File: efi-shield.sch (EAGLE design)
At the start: 117 parts, among them J1 PWMH, J10 MOLEX-85505-5002, J2 PWMI, J3 COMM, J4 PWR, J5 ADCL, J6 ADCH, J7 AMPSEAL-23POS-HEADER, J8 SPI, J9 MOLEX-85505-5002, Q1 PN2222A, Q2 FJPF13009, Q3 PN2222A, Q4 PN2222A, Q5 PN2222A, Q6 PN2222A, SW1 CTS-204-211ST, U1 TXS0104E, U10 MCP2551-I/SN, U2 TXS0104E, U3 MCP3304, U4 MCP6024, U5 MCP6024, U6 MCP6022, U7 NE555DR, U8 MCP4142-104, U9 MCP4142-103

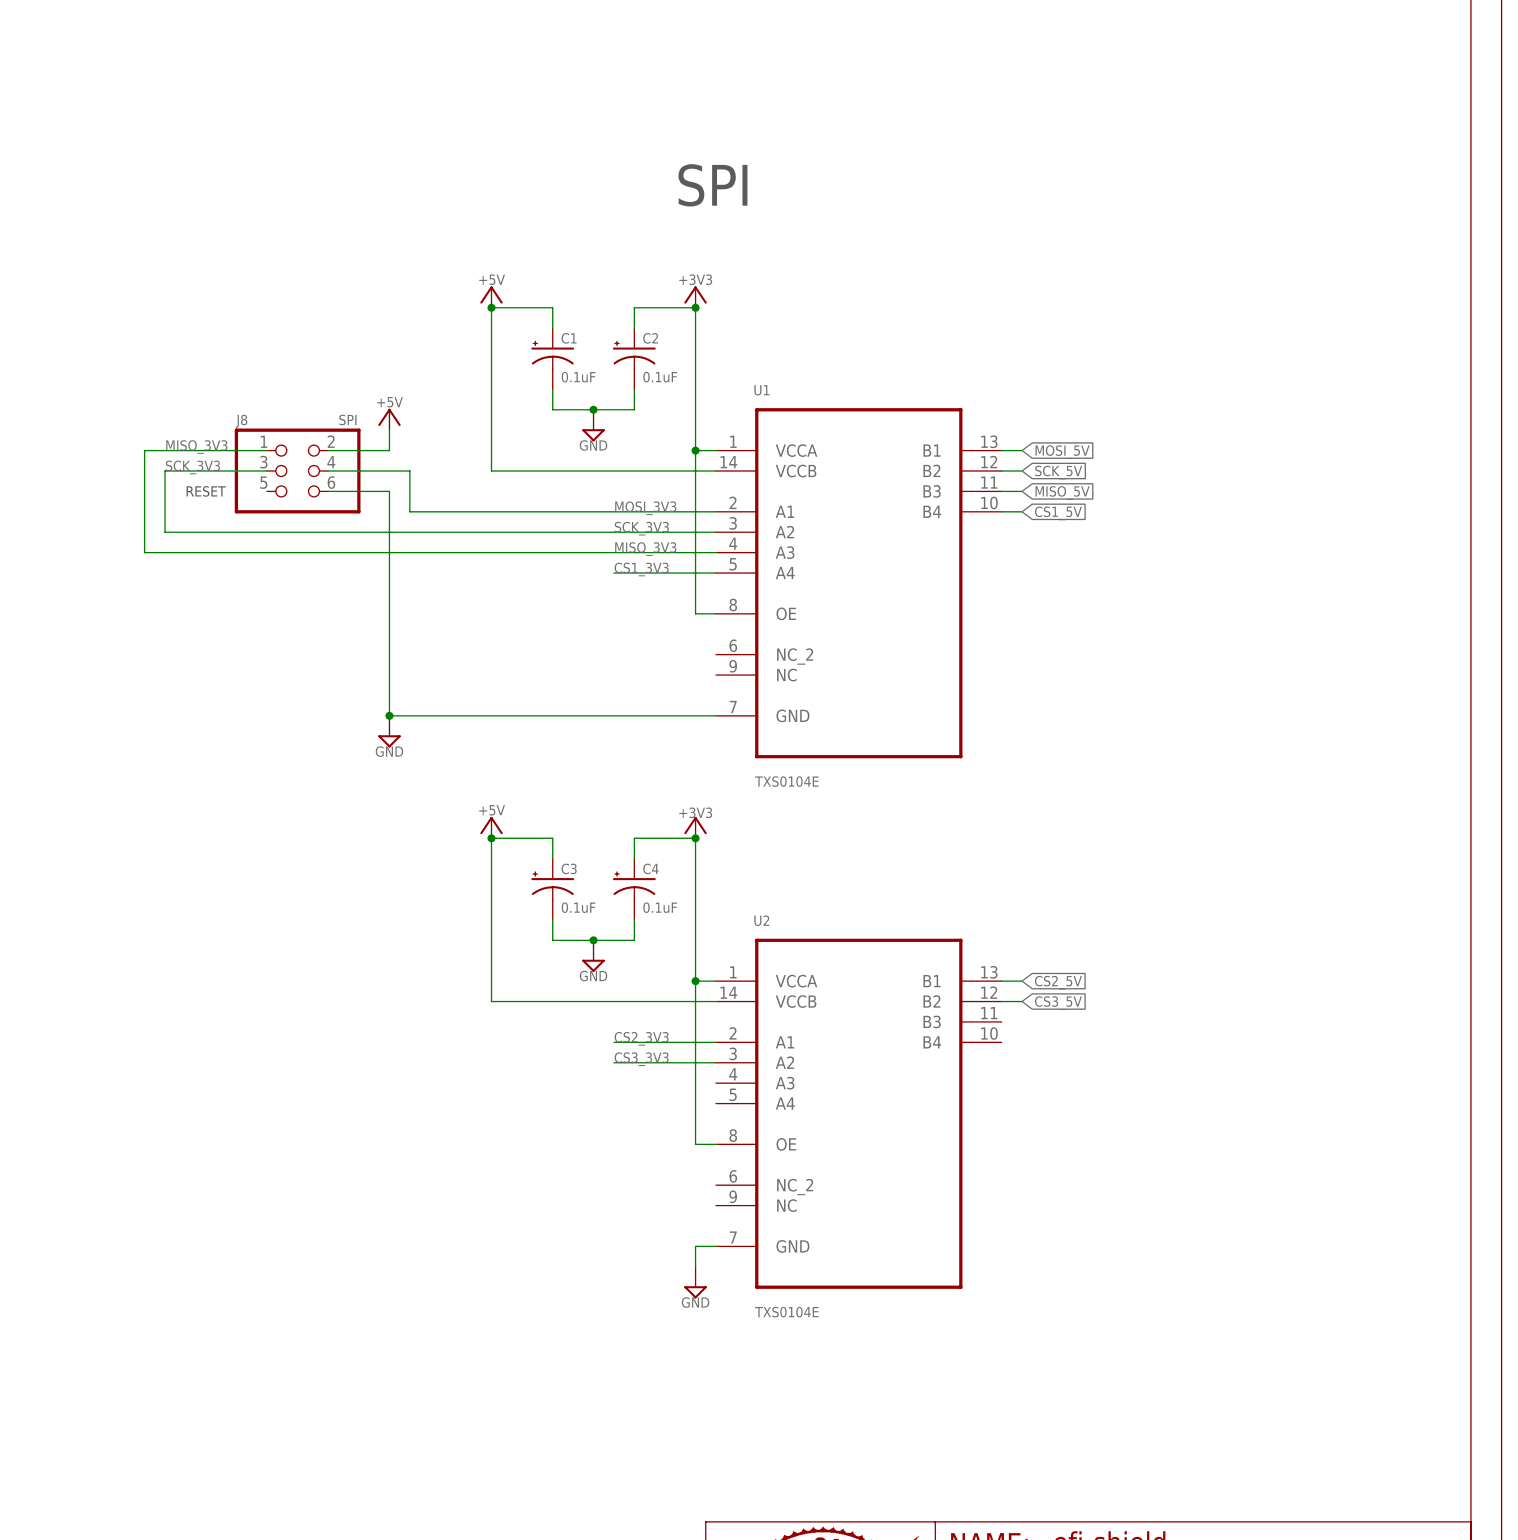
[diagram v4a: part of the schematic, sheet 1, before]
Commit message: Test points and 0ohm filter resistors.
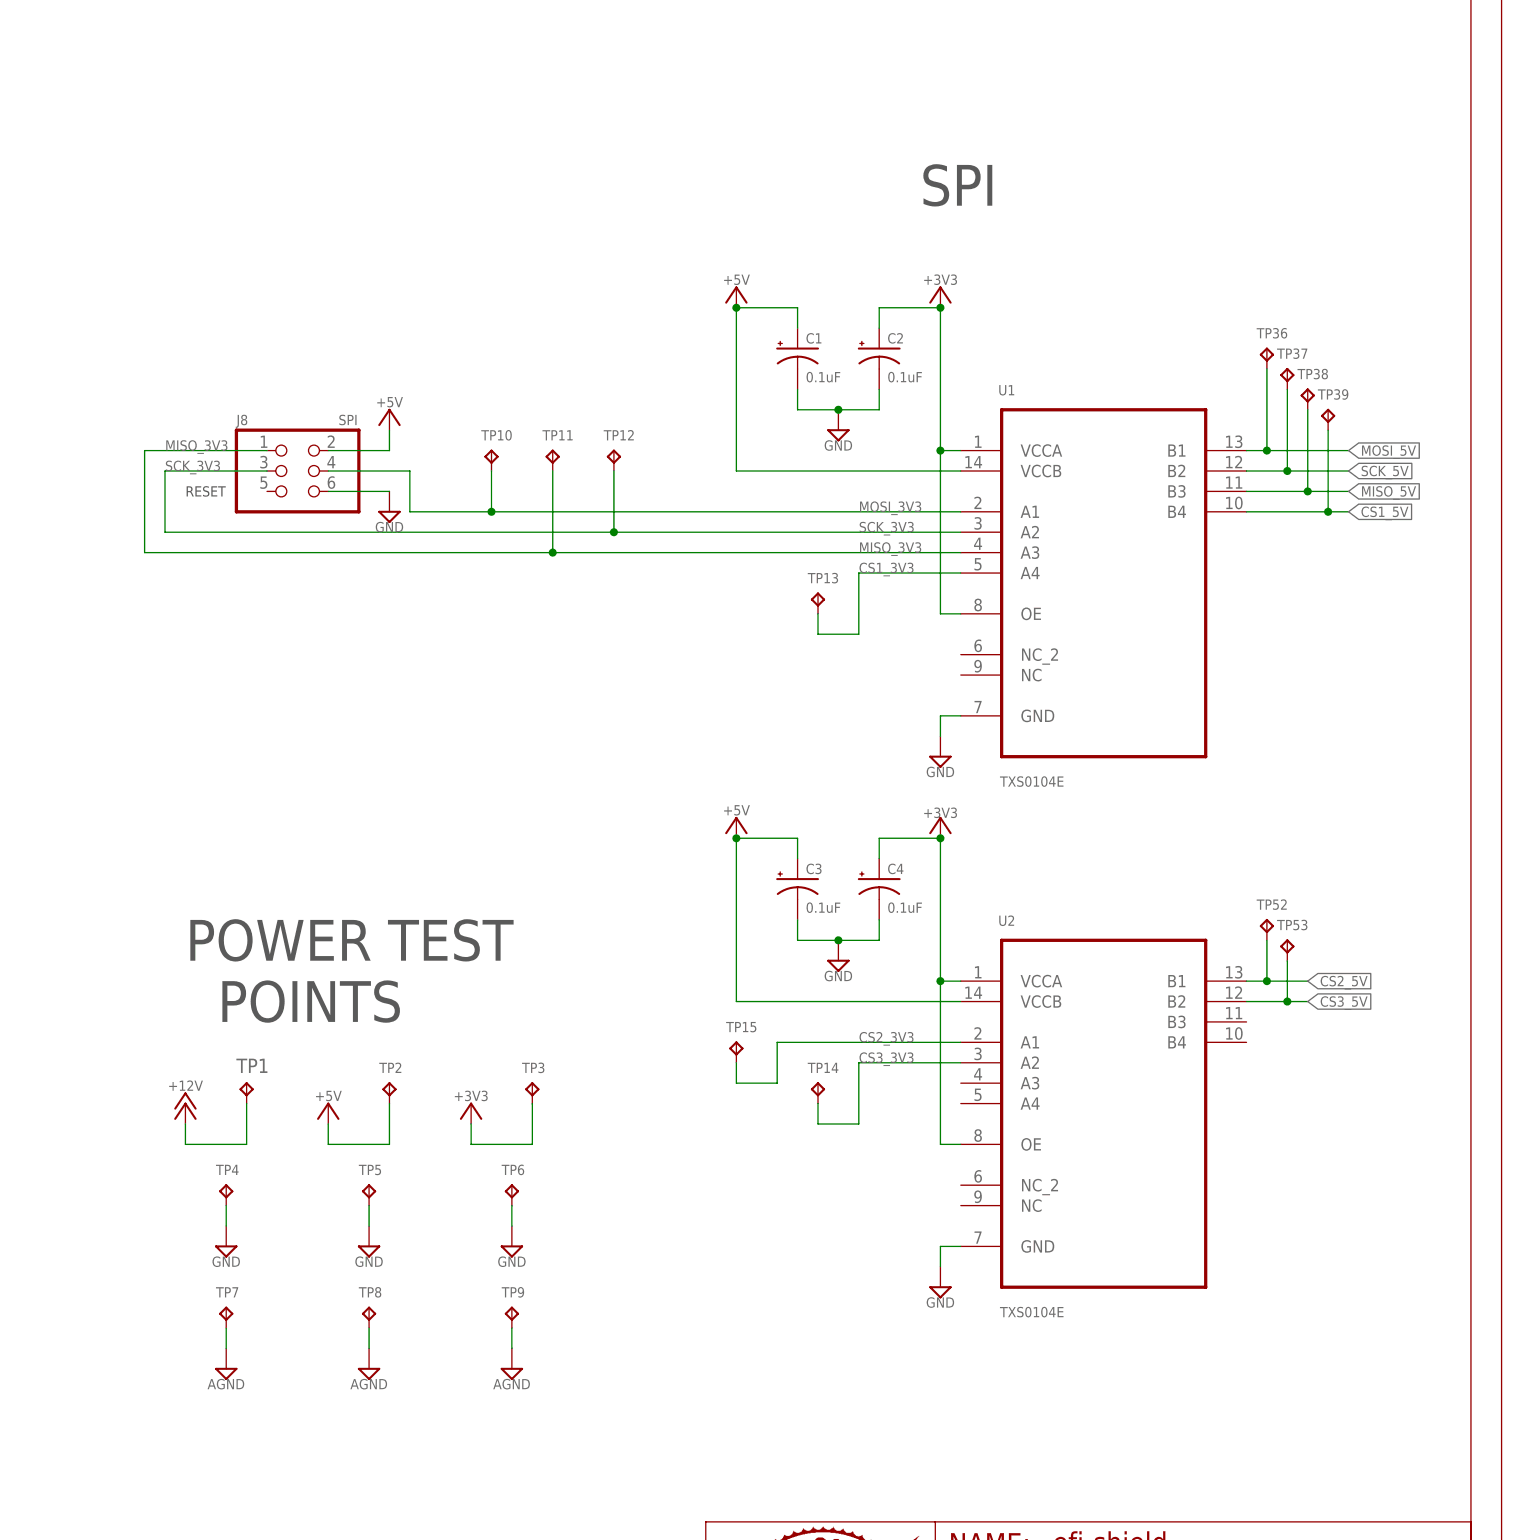
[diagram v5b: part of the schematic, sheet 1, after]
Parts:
- added R37, R38, R39, R40, R41, R42, R43, R44, R45: 0Ω, cpsmv:RES-JKE
- added TP1, TP10, TP11, TP12, TP13, TP14, TP15, TP16, TP17, TP18, TP19, TP2, TP20, TP21, TP22, TP23, TP24, TP25, TP26, TP27, TP28, TP29, TP3, TP30, TP31, TP32, TP33, TP34, TP35, TP36, TP37, TP38, TP39, TP4, TP40, TP41, TP42, TP43, TP44, TP45, TP46, TP47, TP48, TP49, TP5, TP50, TP51, TP52, TP53, TP6, TP7, TP8, TP9: (no value), cpsmv:TEST-POINT
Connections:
- new net ECT_ADC: R40.2, U3.CH3
- new net IAT_ADC: R39.2, U3.CH2
- new net MAP_ADC: R37.2, U3.CH0
- new net N$45: R45.2, U7.TRIG
- new net O2_ADC: R41.2, U3.CH4
- new net SPRA1ADC: R42.2, U3.CH5
- new net SPRA2ADC: R43.2, U3.CH6
- new net SPRA3ADC: R44.2, U3.CH7
- new net TPS_ADC: R38.2, U3.CH1
- net +12V: now also TP1.TP
- net +3V3: now also TP3.TP
- net +5V: now also TP2.TP
- net AGND: now also TP7.TP, TP8.TP, TP9.TP
- net CANH: now also TP44.TP
- net CANL: now also TP45.TP
- net CAN_RX: now also TP47.TP
- net CAN_TX: now also TP46.TP
- net CS1_3V3: now also TP13.TP
- net CS1_5V: now also TP39.TP
- net CS2_3V3: now also TP15.TP
- net CS2_5V: now also TP52.TP
- net CS3_3V3: now also TP14.TP
- net CS3_5V: now also TP53.TP
- net ECT: now also TP26.TP
- net ECT_FIL: now also R40.1, TP27.TP; no longer U3.CH3
- net FUEL: now also TP16.TP
- net FUEL_LED: now also TP49.TP
- net GND: now also TP4.TP, TP5.TP, TP6.TP
- net HALL: now also TP40.TP
- net HALL_FIL: now also R45.1, TP41.TP; no longer U7.TRIG
- net IAT: now also TP24.TP
- net IAT_FIL: now also R39.1, TP25.TP; no longer U3.CH2
- net KILL_SW_LED: now also TP51.TP
- net MAP: now also TP20.TP
- net MAP_FIL: now also R37.1, TP21.TP; no longer U3.CH0
- net MISO_3V3: now also TP11.TP
- net MISO_5V: now also TP38.TP
- net MOSI_3V3: now also TP10.TP
- net MOSI_5V: now also TP36.TP
- net N$38: now also TP19.TP
- net N$39: now also TP17.TP
- net O2: now also TP28.TP
- net O2_FIL: now also R41.1, TP29.TP; no longer U3.CH4
- net REV_LIMIT_LED: now also TP50.TP
- net SCK_3V3: now also TP12.TP
- net SCK_5V: now also TP37.TP
- net SPARK: now also TP18.TP
- net SPARK_LED: now also TP48.TP
- net SPR_A1: now also TP30.TP
- net SPR_A1_FIL: now also R42.1, TP31.TP; no longer U3.CH5
- net SPR_A2: now also TP32.TP
- net SPR_A2_FIL: now also R43.1, TP33.TP; no longer U3.CH6
- net SPR_A3: now also TP34.TP
- net SPR_A3_FIL: now also R44.1, TP35.TP; no longer U3.CH7
- net TACH_3V3: now also TP43.TP
- net TACH_5V: now also TP42.TP
- net TPS: now also TP22.TP
- net TPS_FIL: now also R38.1, TP23.TP; no longer U3.CH1
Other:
- note added: "LAYOUT NOTE: Place CAN termination as close as possible to RJ45 connectors for best CAN performance."
- note added: "POWER TEST POINTS"
- moved on the sheet: C1, C2, C24, C3, C4, Q1, Q2, Q7, R1, R31, R32, U1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

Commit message: Minor updates + schematic PDF.
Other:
- note added: "RJ45 CONNECTORS"
- note added: "TERMINATION"
- note added: "TRANSCEIVER"
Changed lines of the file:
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@@
 CANRX
 CANTX</text>
-<text x="139.7" y="193.04" size="5.08" layer="97">ARDUINO DUE</text>
-<text x="43.18" y="193.04" size="5.08" layer="97">AMPSEAL </text>
+<text x="139.7" y="193.04" size="5.08" layer="97" font="vector">ARDUINO DUE</text>
+<text x="43.18" y="193.04" size="5.08" layer="97" font="vector">AMPSEAL </text>
 <text x="223.52" y="157.48" size="1.27" layer="97" align="center-left">RESET</text>
-<text x="314.96" y="193.04" size="5.08" layer="97">SPI</text>
-<text x="20.32" y="99.06" size="5.08" layer="97">SPARE INPUTS</text>
+<text x="314.96" y="193.04" size="5.08" layer="97" font="vector">SPI</text>
+<text x="20.32" y="99.06" size="5.08" layer="97" font="vector">SPARE INPUTS</text>
 <text x="336.55" y="15.24" size="2.54" layer="94" font="vector">Alex Pink</text>
 <text x="361.95" y="5.08" size="2.54" layer="94" font="vector">01</text>
 <text x="334.01" y="20.32" size="2.54" layer="94" font="vector">Connectors &amp; SPI</text>
-<text x="223.52" y="91.44" size="5.08" layer="97">POWER TEST
+<text x="223.52" y="91.44" size="5.08" layer="97" font="vector">POWER TEST
   POINTS</text>
 </plain>
@@
 <description>ACTUATORS</description>
 <plain>
-<text x="190.5" y="186.69" size="5.08" layer="97">FUEL</text>
+<text x="190.5" y="186.69" size="5.08" layer="97" font="vector">FUEL</text>
 <text x="336.55" y="15.24" size="2.54" layer="94" font="vector">Alex Pink</text>
 <text x="361.95" y="5.08" size="2.54" layer="94" font="vector">01</text>
 <text x="334.01" y="20.32" size="2.54" layer="94" font="vector">Actutators</text>
-<text x="187.96" y="123.19" size="5.08" layer="97">SPARK</text>
+<text x="187.96" y="123.19" size="5.08" layer="97" font="vector">SPARK</text>
 </plain>
 <instances>
@@
 <wire x1="194.31" y1="135.89" x2="194.31" y2="127" width="0.1524" layer="97"/>
 <wire x1="194.31" y1="127" x2="193.04" y2="125.73" width="0.1524" layer="97"/>
-<text x="124.46" y="203.2" size="5.08" layer="97">LOW PASS FILTERS</text>
-<text x="297.18" y="175.26" size="5.08" layer="97">ADC</text>
+<text x="124.46" y="203.2" size="5.08" layer="97" font="vector">LOW PASS FILTERS</text>
+<text x="297.18" y="175.26" size="5.08" layer="97" font="vector">ADC</text>
 <text x="336.55" y="15.24" size="2.54" layer="94" font="vector">Alex Pink</text>
 <text x="361.95" y="5.08" size="2.54" layer="94" font="vector">01</text>
@@
 <text x="361.95" y="5.08" size="2.54" layer="94" font="vector">01</text>
 <text x="334.01" y="20.32" size="2.54" layer="94" font="vector">Tach</text>
-<text x="60.96" y="198.12" size="5.08" layer="97">LOW PASS FILTER</text>
+<text x="60.96" y="198.12" size="5.08" layer="97" font="vector">LOW PASS FILTER</text>
 <text x="55.88" y="185.42" size="1.27" layer="97" font="vector" align="top-left">LAYOUT NOTE:
 Place decoupling caps
@@
 <wire x1="158.75" y1="189.23" x2="158.75" y2="177.8" width="0.1524" layer="97"/>
 <wire x1="158.75" y1="177.8" x2="157.48" y2="176.53" width="0.1524" layer="97"/>
-<text x="271.78" y="134.62" size="5.08" layer="97">555 TIMER</text>
-<text x="165.1" y="198.12" size="5.08" layer="97">   DIGITAL
+<text x="271.78" y="134.62" size="5.08" layer="97" font="vector">555 TIMER</text>
+<text x="165.1" y="198.12" size="5.08" layer="97" font="vector">   DIGITAL
 POTENTIOMETERS</text>
 <text x="274.32" y="76.2" size="1.27" layer="97" font="vector" align="top-left">This capacitor should be
@@
 <wire x1="171.45" y1="118.11" x2="171.45" y2="106.68" width="0.1524" layer="97"/>
 <wire x1="171.45" y1="106.68" x2="170.18" y2="105.41" width="0.1524" layer="97"/>
+<text x="124.46" y="170.18" size="5.08" layer="97" font="vector">TRANSCEIVER</text>
+<text x="167.64" y="81.28" size="5.08" layer="97" font="vector">TERMINATION</text>
+<text x="233.68" y="190.5" size="5.08" layer="97" font="vector">RJ45 CONNECTORS</text>
 </plain>
 <instances>
@@
 <text x="361.95" y="5.08" size="2.54" layer="94" font="vector">01</text>
 <text x="334.01" y="20.32" size="2.54" layer="94" font="vector">LEDs</text>
-<text x="93.98" y="147.32" size="5.08" layer="97">POWER</text>
-<text x="180.34" y="170.18" size="5.08" layer="97">SPARK LED</text>
-<text x="180.34" y="129.54" size="5.08" layer="97">FUEL LED</text>
-<text x="284.48" y="170.18" size="5.08" layer="97">REV LIMIT LED</text>
-<text x="284.48" y="129.54" size="5.08" layer="97">KILLSWITCH LED</text>
+<text x="93.98" y="147.32" size="5.08" layer="97" font="vector">POWER</text>
+<text x="180.34" y="170.18" size="5.08" layer="97" font="vector">SPARK LED</text>
+<text x="180.34" y="129.54" size="5.08" layer="97" font="vector">FUEL LED</text>
+<text x="284.48" y="170.18" size="5.08" layer="97" font="vector">REV LIMIT LED</text>
+<text x="284.48" y="129.54" size="5.08" layer="97" font="vector">KILLSWITCH LED</text>
 </plain>
 <instances>

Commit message: Initial PCB commit.
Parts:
- removed U$1, U$2, U$3, U$4, U$5, U$6: CPSMV-FRAME, cpsmv:CPSMV-FRAME
- Q7: value (none) -> ISL9V5036P3_F085
- TP1: value (none) -> +12V
- TP10: value (none) -> MOSI_3V3
- TP11: value (none) -> MISO_3V3
- TP12: value (none) -> SCK_3V3
- TP13: value (none) -> CS1_3V3
- TP14: value (none) -> CS3_3V3
- TP15: value (none) -> CS2_3V3
- TP16: value (none) -> FUEL
- TP17: value (none) -> FUEL_E
- TP18: value (none) -> SPARK
- TP19: value (none) -> SPARK_E
- TP2: value (none) -> +5V
- TP20: value (none) -> MAP
- TP21: value (none) -> MAP_FIL
- TP22: value (none) -> TPS
- TP23: value (none) -> TPS_FIL
- TP24: value (none) -> IAT
- TP25: value (none) -> IAT_FIL
- TP26: value (none) -> ECT
- TP27: value (none) -> ECT_FIL
- TP28: value (none) -> O2
- TP29: value (none) -> O2_FIL
- TP3: value (none) -> +3V3
- TP30: value (none) -> SPR_A1
- TP31: value (none) -> SPR_A1_FIL
- TP32: value (none) -> SPR_A2
- TP33: value (none) -> SPR_A2_FIL
- TP34: value (none) -> SPR_A3
- TP35: value (none) -> SPR_A3_FIL
- TP36: value (none) -> MOSI_5V
- TP37: value (none) -> SCK_5V
- TP38: value (none) -> MISO_5V
- TP39: value (none) -> CS1_5V
- TP4, TP5, TP6: value (none) -> GND
- TP40: value (none) -> HALL
- TP41: value (none) -> HALL_FIL
- TP42: value (none) -> TACH_5V
- TP43: value (none) -> TACH_3V3
- TP44: value (none) -> CANH
- TP45: value (none) -> CANL
- TP46: value (none) -> CAN_TX
- TP47: value (none) -> CAN_RX
- TP48: value (none) -> SPARK_LED
- TP49: value (none) -> FUEL_LED
- TP50: value (none) -> REV_LIMIT_LED
- TP51: value (none) -> KILL_SW_LED
- TP52: value (none) -> CS2_5V
- TP53: value (none) -> CS3_5V
- TP7, TP8, TP9: value (none) -> AGND

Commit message: Low-impedance termination tach circuitadded. Removed one-shot/digi-pot and LPF tach circuit.
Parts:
- removed C26, C27: 330pF, cpsmv:CAP-JKE
- removed C28, C29: 10nF, cpsmv:CAP-JKE
- removed C30, C31, C32: 0.1uF, cpsmv:CAP-JKE
- removed R18, R19: 100kΩ, cpsmv:RES-JKE
- removed R45: 0Ω, cpsmv:RES-JKE
- removed TP40: HALL, cpsmv:TEST-POINT
- removed TP41: HALL_FIL, cpsmv:TEST-POINT
- removed TP42: TACH_5V, cpsmv:TEST-POINT
- removed TP43: TACH_3V3, cpsmv:TEST-POINT
- removed U6: MCP6022, cpsmv:MCP6022-I/SN
- removed U7: NE555DR, cpsmv:NE555DR
- removed U8: MCP4142-104, cpsmv:MCP4142-104E/P
- removed U9: MCP4142-103, cpsmv:MCP4142-103E/P
- C25: value 47nF -> 68nF
- R20: value 36kΩ -> 220Ω
- R21: value 64kΩ -> 390Ω
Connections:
- removed net HALL_FIL: C26.1, R45.1, TP41.TP, U6.VINA-, U6.VOUTA
- removed net N$13: C27.1, R19.2, U6.VINA+
- removed net N$22: C26.2, R18.2, R19.1
- removed net N$23: U8.P0B, U9.P0W
- removed net N$24: C29.1, U7.CONT
- removed net N$4: C32.1, U7.DISCH, U7.THRES, U9.P0B
- removed net N$45: R45.2, U7.TRIG
- removed net TACH_3V3: J2.3, R20.2, R21.2, TP43.TP
- removed net TACH_5V: R20.1, TP42.TP, U7.OUT
- net +5V: now also R20.2; no longer C25.1, C28.1, C30.1, C31.1, U6.VDD, U7.RESET, U7.VCC, U8.P0W, U8.VDD, U9.VDD
- net AGND: no longer C25.2, C27.2, U6.VSS
- net CS2_5V: no longer U8.~CS
- net CS3_5V: no longer U9.~CS
- net GND: now also C25.2; no longer C28.2, C29.2, C30.2, C31.2, C32.2, U7.GND, U8.VSS, U9.VSS
- net HALL: now also C25.1, J2.3, R20.1, R21.2; no longer R18.1, TP40.TP
- net MISO_5V: no longer U8.SDO, U9.SDO
- net MOSI_5V: no longer U8.SDI, U9.SDI
- net SCK_5V: no longer U8.SCK, U9.SCK
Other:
- note added: "HIGH FREQ BLOCKER"
- note added: "LOW IMPEDANCE TERMINATION"
- note added: "PULLUP"
- note added: "TACH"
- note added: "Tach + CAN"
- note removed: "555 TIMER"
- note removed: "DIGITAL POTENTIOMETERS"
- note removed: "LAYOUT NOTE: Place within 100mm of 1uf buld capacitor shared with other MCP602x devices."
- note removed: "LOW PASS FILTER"
- note removed: "Tach"
- note removed: "This capacitor should be changed per the trigger wheel/timing sensor configuration of the engine. Rough parameters: Single tooth - 1.0uF 12+ teeth - 0.1uF"
